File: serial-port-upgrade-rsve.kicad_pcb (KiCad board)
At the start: 2 copper layers, 12 parts, among them J1 MFP RC, J2 MFP TDO, J3 VCC, J4 GND, J5 Led, U1 GAL16V8_PHY, U2 12-STAGE_BINARY_RIPPLE_COUNTE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, X1 1,8432 MHz

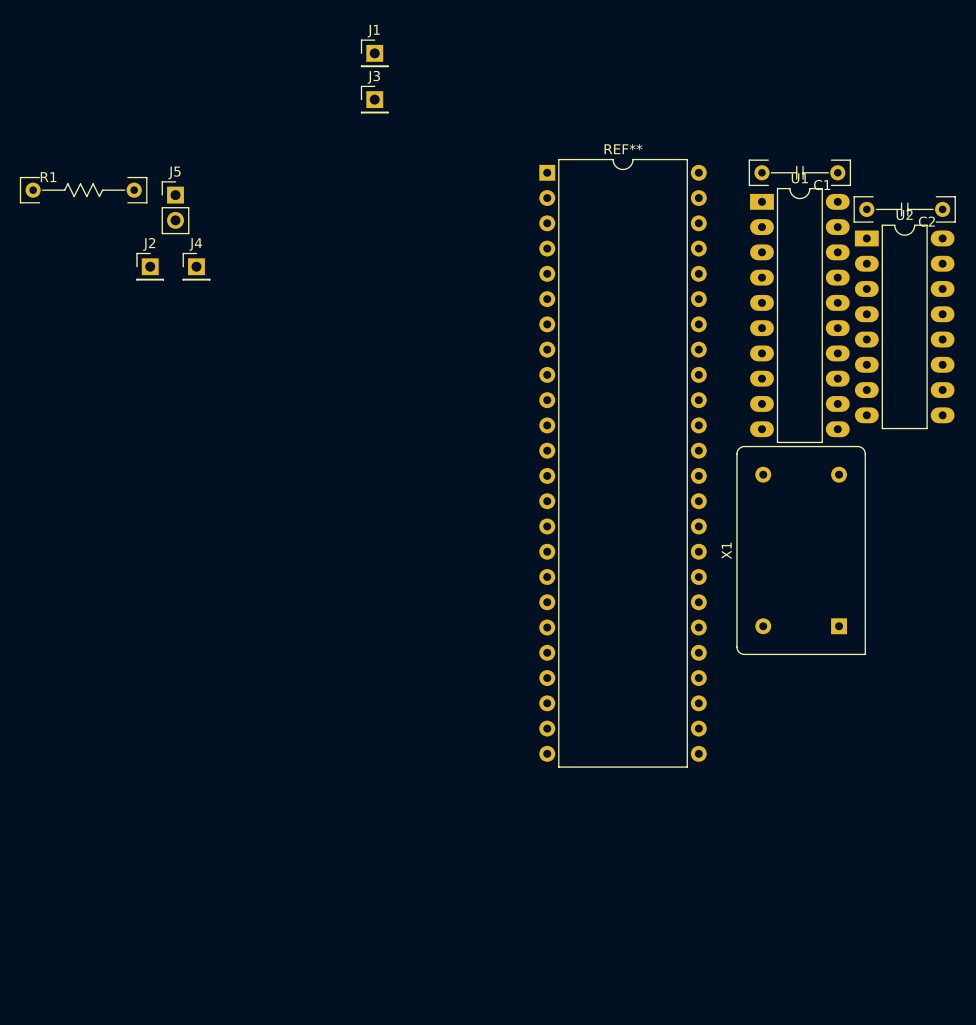
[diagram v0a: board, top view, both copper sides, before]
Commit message: added reference layout, place components
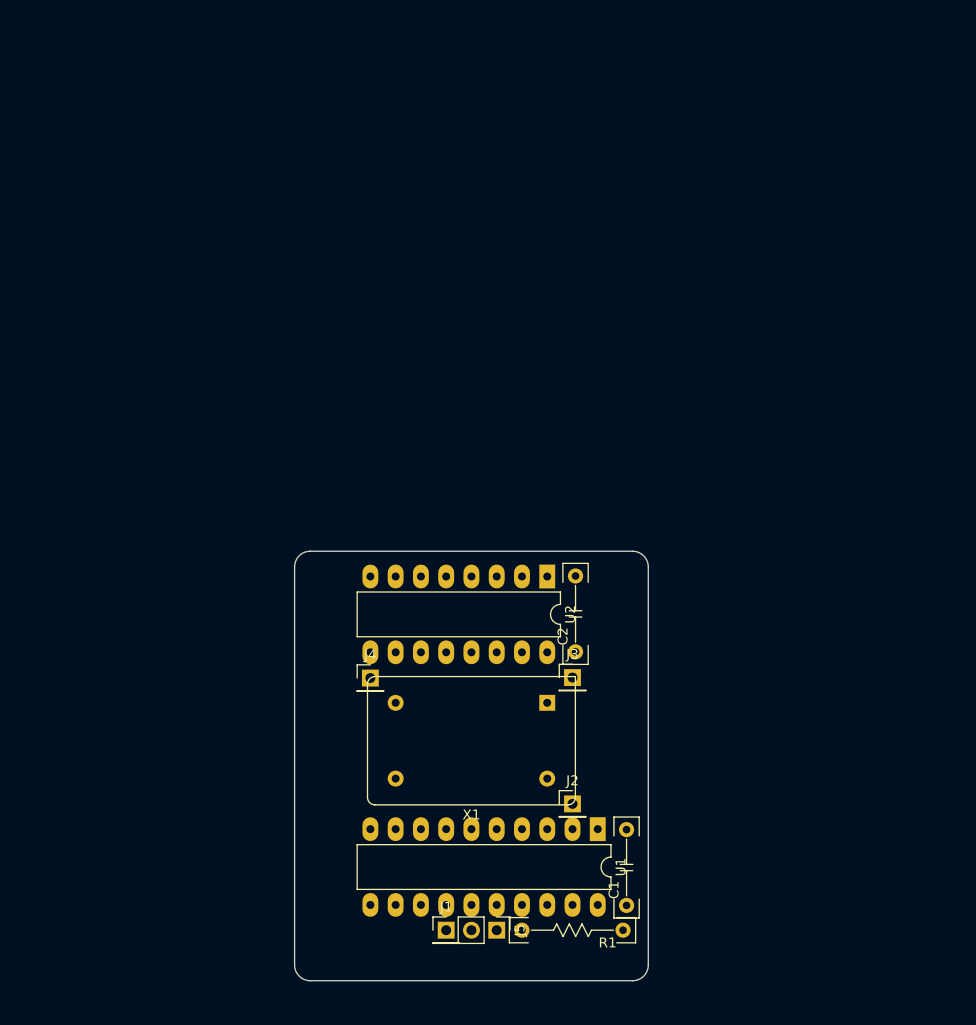
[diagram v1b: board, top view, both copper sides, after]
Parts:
- removed REF**: DIP-48_W15.24mm, Package_DIP:DIP-48_W15.24mm
- added G***: LOGO, rsve:silkscreen, F.Cu at (94.1, 97.8)
- added G***: LOGO, rsve:bottom-side, F.Cu at (94.1, 97.8)
- moved R1 89.2 mm to (104.1, 114.2), turned to 180 degrees
- moved J1 88.4 mm to (91.4, 114.2)
- moved J5 80.7 mm to (96.5, 114.2), turned to 270 degrees
- moved C1 72.0 mm to (109.6, 108.0), turned to 90 degrees
- moved J2 68.7 mm to (104.1, 101.5)
- moved U1 65.2 mm to (106.7, 104.1), turned to 270 degrees
- moved J3 61.4 mm to (104.1, 88.8)
- moved C2 52.4 mm to (104.4, 82.4), turned to 90 degrees
- moved U2 46.8 mm to (101.6, 78.7), turned to 270 degrees
- moved J4 44.9 mm to (83.8, 88.9)
- moved X1 30.3 mm to (101.6, 91.4), turned to 180 degrees
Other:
- board outline added: 35.6 x 43.2 mm

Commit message: setup pcb stack
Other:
- copper layers 2 -> 4
- net class Clock added: clearance 0.4064, trace_width 0.2032, via_dia 0.8128, via_drill 0.4064
- net class Default: clearance 0.2 -> 0.2032; trace_width 0.25 -> 0.2032; via_dia 0.8 -> 0.8128; via_drill 0.4 -> 0.4064
- net class Power added: clearance 0.2032, trace_width 1.016, via_dia 0.8128, via_drill 0.4064
- rule trace_clearance: 0.2 -> 0.2032
- rule trace_min: 0.2 -> 0.127
- rule via_min_drill: 0.3 -> 0.254
- rule via_min_size: 0.4 -> 0.381
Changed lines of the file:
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@@
   (layers
     (0 F.Cu signal)
+    (1 In1.Cu signal)
+    (2 In2.Cu signal)
     (31 B.Cu signal)
     (32 B.Adhes user)
@@
   )
   (setup
-    (last_trace_width 0.25)
-    (trace_clearance 0.2)
+    (last_trace_width 0.2032)
+    (user_trace_width 0.2032)
+    (user_trace_width 1.016)
+    (trace_clearance 0.2032)
     (zone_clearance 0.508)
     (zone_45_only no)
-    (trace_min 0.2)
-    (via_size 0.8)
-    (via_drill 0.4)
-    (via_min_size 0.4)
-    (via_min_drill 0.3)
-    (uvia_size 0.3)
-    (uvia_drill 0.1)
+    (trace_min 0.127)
+    (via_size 0.8128)
+    (via_drill 0.4064)
+    (via_min_size 0.381)
+    (via_min_drill 0.254)
+    (user_via 0.8128 0.4064)
+    (uvia_size 0.2032)
+    (uvia_drill 0.1016)
     (uvias_allowed no)
-    (uvia_min_size 0.2)
-    (uvia_min_drill 0.1)
+    (uvia_min_size 0.2032)
+    (uvia_min_drill 0.1016)
     (edge_width 0.05)
     (segment_width 0.2)
@@
   (net 26 "Net-(X1-Pad1)")
   (net_class Default "Ceci est la Netclass par défaut."
-    (clearance 0.2)
-    (trace_width 0.25)
-    (via_dia 0.8)
-    (via_drill 0.4)
-    (uvia_dia 0.3)
-    (uvia_drill 0.1)
-    (add_net /clk)
+    (clearance 0.2032)
+    (trace_width 0.2032)
+    (via_dia 0.8128)
+    (via_drill 0.4064)
+    (uvia_dia 0.2032)
+    (uvia_drill 0.1016)
     (add_net /cp)
     (add_net /led+)
@@
     (add_net /tid)
     (add_net /tua)
-    (add_net GND)
     (add_net "Net-(U1-Pad16)")
     (add_net "Net-(U1-Pad17)")
@@
     (add_net "Net-(U2-Pad9)")
     (add_net "Net-(X1-Pad1)")
+  )
+  (net_class Clock ""
+    (clearance 0.4064)
+    (trace_width 0.2032)
+    (via_dia 0.8128)
+    (via_drill 0.4064)
+    (uvia_dia 0.2032)
+    (uvia_drill 0.1016)
+    (add_net /clk)
+  )
+  (net_class Power ""
+    (clearance 0.2032)
+    (trace_width 1.016)
+    (via_dia 0.8128)
+    (via_drill 0.4064)
+    (uvia_dia 0.2032)
+    (uvia_drill 0.1016)
+    (add_net GND)
     (add_net VCC)
   )

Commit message: done routing
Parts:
- moved C1 0.41 mm to (109.2, 108.0)
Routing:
- net VCC: track 0.00 -> 36.6 mm
- net /clk: track 0.00 -> 30.4 mm
- net /mr: track 0.00 -> 27.5 mm
- net /cp: track 0.00 -> 26.5 mm
- net Net-(U1-Pad7): track 0.00 -> 26.3 mm
- net Net-(U1-Pad6): track 0.00 -> 26.3 mm
- net Net-(U1-Pad5): track 0.00 -> 26.3 mm
- net Net-(U1-Pad4): track 0.00 -> 26.3 mm
- net /q7: track 0.00 -> 24.9 mm
- net /tua: track 0.00 -> 2.54 mm
- net /tid: track 0.00 -> 2.54 mm
- net /led-: track 0.00 -> 2.54 mm
- net /led+: track 0.00 -> 2.54 mm
- added copper zone on In2.Cu, net (none)
- added copper zone on B.Cu, net GND
- added copper zone on F.Cu, net GND
- added copper zone on In1.Cu, net GND
- added copper zone on B.Cu, net VCC
- added copper zone on F.Cu, net VCC
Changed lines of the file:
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@@
     (thickness 1.6)
     (drawings 8)
-    (tracks 0)
+    (tracks 53)
     (zones 0)
     (modules 13)
@@
     (40 Dwgs.User user)
     (41 Cmts.User user)
-    (42 Eco1.User user)
-    (43 Eco2.User user)
+    (42 Eco1.User user hide)
+    (43 Eco2.User user hide)
     (44 Edge.Cuts user)
     (45 Margin user)
@@
     (user_trace_width 1.016)
     (trace_clearance 0.2032)
-    (zone_clearance 0.508)
+    (zone_clearance 0.254)
     (zone_45_only no)
     (trace_min 0.127)
@@
   )
   (module commons-passives_THT:Passive_THT_capacitor_mlcc_W2.54mm_L7.62mm (layer F.Cu)
-    (at 109.5756 107.95 90)
+    (at 109.1692 107.95 90)
     (descr "MLCC THT axial capacitor, width 100mils, lead vias 300mils apart")
     (tags "mlcc axial capacitor tht")
@@
   (gr_arc (start 77.7748 117.7544) (end 76.2 117.7544) (angle -90) (layer Edge.Cuts) (width 0.05))
   (gr_arc (start 77.7748 77.724) (end 77.7748 76.1492) (angle -90) (layer Edge.Cuts) (width 0.05))
+  (segment (start 104.4448 88.5444) (end 104.14 88.8492) (width 1.016) (layer B.Cu) (net 2))
+  (segment (start 104.4448 86.2584) (end 104.4448 88.5444) (width 1.016) (layer B.Cu) (net 2))
+  (segment (start 104.14 96.4692) (end 101.6 99.0092) (width 1.016) (layer B.Cu) (net 2))
+  (segment (start 104.14 88.8492) (end 104.14 96.4692) (width 1.016) (layer B.Cu) (net 2))
+  (segment (start 106.7308 111.76) (end 106.68 111.7092) (width 1.016) (layer B.Cu) (net 2))
+  (segment (start 109.1692 111.76) (end 106.7308 111.76) (width 1.016) (layer B.Cu) (net 2))
+  (segment (start 101.6 99.0092) (end 101.6 104.0892) (width 1.016) (layer B.Cu) (net 2))
+  (segment (start 109.1692 114.1984) (end 109.22 114.2492) (width 1.016) (layer B.Cu) (net 2))
+  (segment (start 109.1692 111.76) (end 109.1692 114.1984) (width 1.016) (layer B.Cu) (net 2))
+  (segment (start 101.6508 86.2584) (end 101.6 86.3092) (width 1.016) (layer B.Cu) (net 2))
+  (segment (start 104.4448 86.2584) (end 101.6508 86.2584) (width 1.016) (layer B.Cu) (net 2))
+  (segment (start 106.68 111.7092) (end 106.68 110.7948) (width 1.016) (layer B.Cu) (net 2))
+  (segment (start 101.6 105.7148) (end 101.6 104.0892) (width 1.016) (layer B.Cu) (net 2))
+  (segment (start 106.68 110.7948) (end 101.6 105.7148) (width 1.016) (layer B.Cu) (net 2))
+  (segment (start 91.44 114.2492) (end 91.44 111.7092) (width 0.2032) (layer F.Cu) (net 3))
+  (segment (start 104.14 104.0892) (end 104.14 101.5492) (width 0.2032) (layer F.Cu) (net 4))
+  (segment (start 93.98 114.2492) (end 93.98 111.7092) (width 0.2032) (layer F.Cu) (net 5))
+  (segment (start 99.06 114.2492) (end 96.52 114.2492) (width 0.2032) (layer F.Cu) (net 6))
+  (segment (start 86.36 99.0092) (end 86.36 104.0892) (width 0.2032) (layer F.Cu) (net 8))
+  (segment (start 86.36 104.0892) (end 86.36 106.3244) (width 0.2032) (layer F.Cu) (net 8))
+  (segment (start 86.36 106.3244) (end 87.3252 107.2896) (width 0.2032) (layer F.Cu) (net 8))
+  (segment (start 87.3252 107.2896) (end 105.2576 107.2896) (width 0.2032) (layer F.Cu) (net 8))
+  (segment (start 106.68 105.8672) (end 106.68 104.0892) (width 0.2032) (layer F.Cu) (net 8))
+  (segment (start 105.2576 107.2896) (end 106.68 105.8672) (width 0.2032) (layer F.Cu) (net 8))
+  (segment (start 93.98 86.3092) (end 93.98 89.8144) (width 0.2032) (layer F.Cu) (net 10))
+  (segment (start 93.98 89.8144) (end 92.71 91.0844) (width 0.2032) (layer F.Cu) (net 10))
+  (segment (start 92.71 91.0844) (end 92.71 105.3592) (width 0.2032) (layer F.Cu) (net 10))
+  (segment (start 92.71 105.3592) (end 91.9988 106.0704) (width 0.2032) (layer F.Cu) (net 10))
+  (segment (start 91.9988 106.0704) (end 90.2716 106.0704) (width 0.2032) (layer F.Cu) (net 10))
+  (segment (start 88.9 104.6988) (end 88.9 104.0892) (width 0.2032) (layer F.Cu) (net 10))
+  (segment (start 90.2716 106.0704) (end 88.9 104.6988) (width 0.2032) (layer F.Cu) (net 10))
+  (segment (start 92.54481 79.79401) (end 92.54481 89.77639) (width 0.2032) (layer F.Cu) (net 12))
+  (segment (start 91.44 78.6892) (end 92.54481 79.79401) (width 0.2032) (layer F.Cu) (net 12))
+  (segment (start 91.44 90.8812) (end 91.44 104.0892) (width 0.2032) (layer F.Cu) (net 12))
+  (segment (start 92.54481 89.77639) (end 91.44 90.8812) (width 0.2032) (layer F.Cu) (net 12))
+  (segment (start 95.08481 79.79401) (end 95.08481 89.77639) (width 0.2032) (layer F.Cu) (net 14))
+  (segment (start 93.98 78.6892) (end 95.08481 79.79401) (width 0.2032) (layer F.Cu) (net 14))
+  (segment (start 93.98 90.8812) (end 93.98 104.0892) (width 0.2032) (layer F.Cu) (net 14))
+  (segment (start 95.08481 89.77639) (end 93.98 90.8812) (width 0.2032) (layer F.Cu) (net 14))
+  (segment (start 97.62481 79.79401) (end 97.62481 89.77639) (width 0.2032) (layer F.Cu) (net 15))
+  (segment (start 96.52 78.6892) (end 97.62481 79.79401) (width 0.2032) (layer F.Cu) (net 15))
+  (segment (start 96.52 90.8812) (end 96.52 104.0892) (width 0.2032) (layer F.Cu) (net 15))
+  (segment (start 97.62481 89.77639) (end 96.52 90.8812) (width 0.2032) (layer F.Cu) (net 15))
+  (segment (start 100.16481 79.79401) (end 100.16481 89.67479) (width 0.2032) (layer F.Cu) (net 16))
+  (segment (start 99.06 78.6892) (end 100.16481 79.79401) (width 0.2032) (layer F.Cu) (net 16))
+  (segment (start 99.06 90.7796) (end 99.06 104.0892) (width 0.2032) (layer F.Cu) (net 16))
+  (segment (start 100.16481 89.67479) (end 99.06 90.7796) (width 0.2032) (layer F.Cu) (net 16))
+  (segment (start 87.79519 110.60439) (end 88.9 111.7092) (width 0.2032) (layer B.Cu) (net 17))
+  (segment (start 87.79519 87.74439) (end 87.79519 110.60439) (width 0.2032) (layer B.Cu) (net 17))
+  (segment (start 86.36 86.3092) (end 87.79519 87.74439) (width 0.2032) (layer B.Cu) (net 17))
+  (segment (start 85.051999 90.157201) (end 88.9 86.3092) (width 0.2032) (layer F.Cu) (net 18))
+  (segment (start 85.051999 110.401199) (end 85.051999 90.157201) (width 0.2032) (layer F.Cu) (net 18))
+  (segment (start 86.36 111.7092) (end 85.051999 110.401199) (width 0.2032) (layer F.Cu) (net 18))
+  (zone (net 1) (net_name GND) (layer In1.Cu) (hatch edge 0.508)
+    (connect_pads (clearance 0.254))
+    (min_thickness 0.254)
+    (fill yes (arc_segments 32) (thermal_gap 0.508) (thermal_bridge_width 0.508))
+    (polygon
+      (pts
+        (xy 112.3188 120.1928) (xy 73.5076 120.1928) (xy 73.5076 73.5076) (xy 112.3188 73.5076)
+      )
+    )
+  )
+  (zone (net 1) (net_name GND) (layer F.Cu) (hatch edge 0.508)
+    (connect_pads (clearance 0.254))
+    (min_thickness 0.254)
+    (fill yes (arc_segments 32) (thermal_gap 0.508) (thermal_bridge_width 0.508))
+    (polygon
+      (pts
+        (xy 114.7064 121.7676) (xy 75.5396 121.7676) (xy 75.5396 75.5396) (xy 114.7064 75.5396)
+      )
+    )
+  )
+  (zone (net 2) (net_name VCC) (layer F.Cu) (hatch edge 0.508)
+    (priority 1)
+    (connect_pads (clearance 0.254))
+    (min_thickness 0.254)
+    (fill yes (arc_segments 32) (thermal_gap 0.508) (thermal_bridge_width 0.508))
+    (polygon
+      (pts
+        (xy 107.4928 115.4684) (xy 80.01 115.4684) (xy 80.01 80.264) (xy 107.4928 80.264)
+      )
+    )
+  )
+  (zone (net 0) (net_name "") (layer In2.Cu) (hatch edge 0.508)
+    (connect_pads (clearance 0.254))
+    (min_thickness 0.254)
+    (fill yes (arc_segments 32) (thermal_gap 0.508) (thermal_bridge_width 0.508))
+    (polygon
+      (pts
+        (xy 113.308131 119.6848) (xy 74.496931 119.6848) (xy 74.496931 72.9996) (xy 113.308131 72.9996)
+      )
+    )
+  )
+  (zone (net 2) (net_name VCC) (layer B.Cu) (hatch edge 0.508)
+    (priority 1)
+    (connect_pads (clearance 0.254))
+    (min_thickness 0.254)
+    (fill yes (arc_segments 32) (thermal_gap 0.508) (thermal_bridge_width 0.508))
+    (polygon
+      (pts
+        (xy 107.4928 115.4684) (xy 80.01 115.4684) (xy 80.01 80.264) (xy 107.4928 80.264)
+      )
+    )
+  )
+  (zone (net 1) (net_name GND) (layer B.Cu) (hatch edge 0.508)
+    (connect_pads (clearance 0.254))
+    (min_thickness 0.254)
+    (fill yes (arc_segments 32) (thermal_gap 0.508) (thermal_bridge_width 0.508))
+    (polygon
+      (pts
+        (xy 114.1476 121.2088) (xy 74.9808 121.2088) (xy 74.9808 74.9808) (xy 114.1476 74.9808)
+      )
+    )
+  )
 )

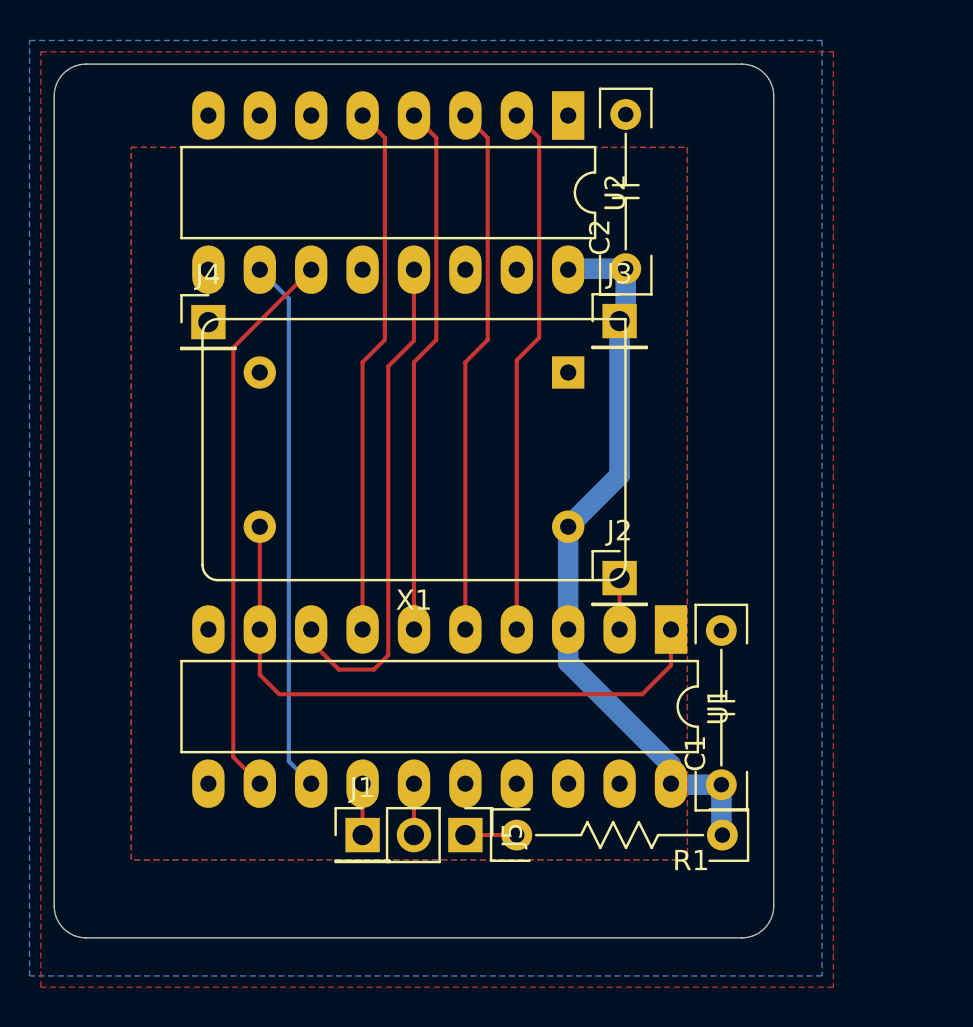
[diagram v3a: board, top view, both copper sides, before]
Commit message: added IDC connector, adjusted reference label position
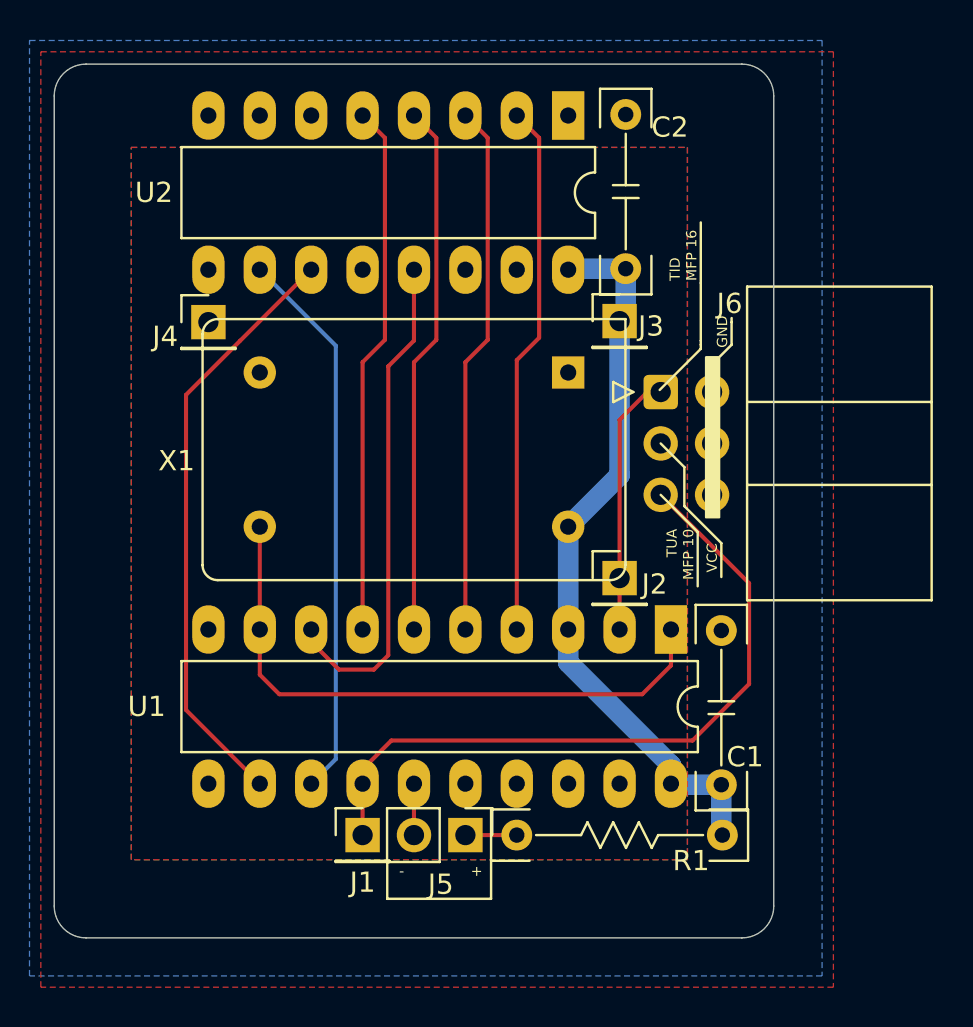
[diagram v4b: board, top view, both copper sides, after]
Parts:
- added J6: IDC connector, Connector_IDC:IDC-Header_2x03_P2.54mm_Horizontal, F.Cu at (106.2, 92.4)
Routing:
- net /tua: track 2.54 -> 35.3 mm
- net /tid: track 2.54 -> 13.0 mm
- net /mr: track 27.5 -> 29.5 mm
- net /cp: track 26.5 -> 27.5 mm
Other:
- board text added: "+"
- board text added: "-"
- board text added: "GND"
- board text added: "TID MFP 16"
- board text added: "TUA MFP 10"
- board text added: "VCC"
